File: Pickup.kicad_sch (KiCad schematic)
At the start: 38 parts, among them U401 PCM1808, U402 PCM1808, U403 PCM1808

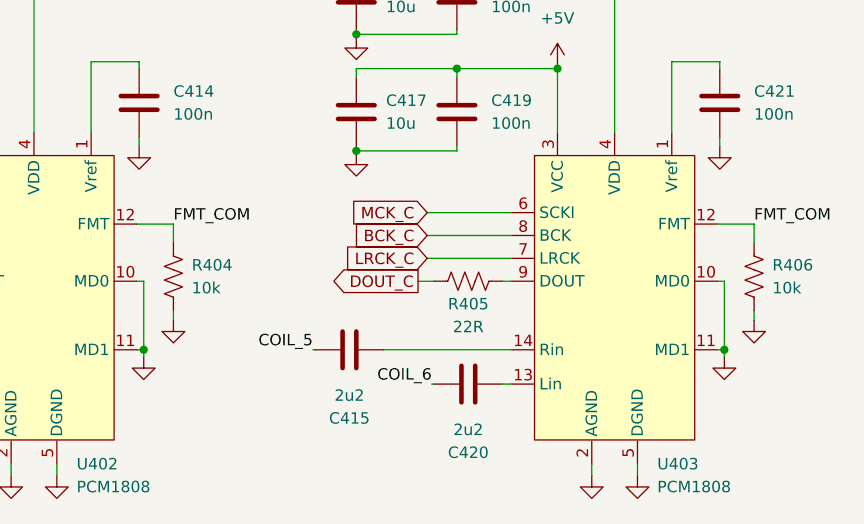
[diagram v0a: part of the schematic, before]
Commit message: installed Semtech LLCC68 RF driver
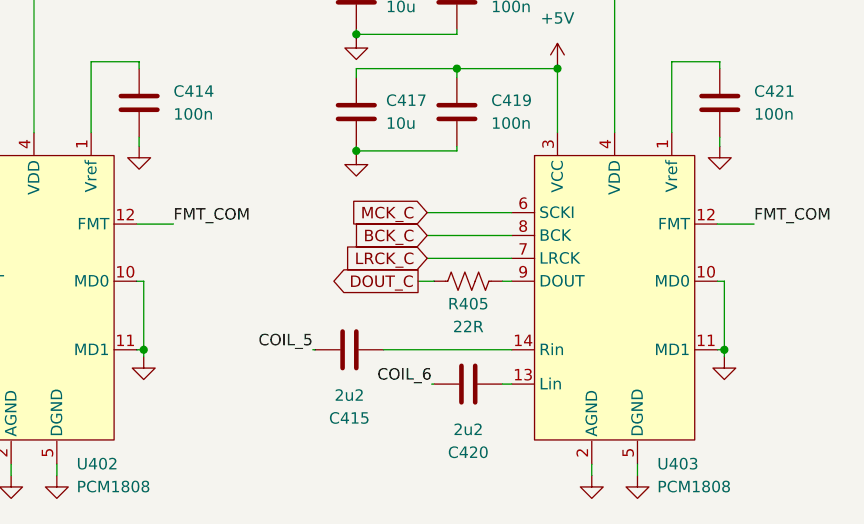
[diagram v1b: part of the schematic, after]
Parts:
- removed R404, R406: 10k, symbol Device:R_US

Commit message: LEDs and footprints
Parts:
- C406, C407, C408, C413, C415, C420: footprint (none) -> Capacitor_SMD:C_0805_2012Metric
- JP401: footprint (none) -> Jumper:SolderJumper-2_P1.3mm_Open_TrianglePad1.0x1.5mm
- L401, L402, L403, L404, L405, L406: footprint (none) -> Inductor_THT:L_Radial_L8.0mm_W8.0mm_P5.00mm_Neosid_SD8
- NT401: footprint (none) -> NetTie:NetTie-2_SMD_Pad0.5mm
- R401, R402, R403, R405: footprint (none) -> Resistor_SMD:R_0805_2012Metric
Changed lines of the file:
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@@
 			)
 		)
-		(property "Footprint" ""
+		(property "Footprint" "Resistor_SMD:R_0805_2012Metric"
 			(at 230.124 93.472 90)
 			(effects
@@
 			)
 		)
-		(property "Footprint" ""
+		(property "Footprint" "Inductor_THT:L_Radial_L8.0mm_W8.0mm_P5.00mm_Neosid_SD8"
 			(at 40.894 85.344 0)
 			(effects
@@
 			)
 		)
-		(property "Footprint" ""
+		(property "Footprint" "Resistor_SMD:R_0805_2012Metric"
 			(at 100.33 94.234 90)
 			(effects
@@
 			)
 		)
-		(property "Footprint" ""
+		(property "Footprint" "Jumper:SolderJumper-2_P1.3mm_Open_TrianglePad1.0x1.5mm"
 			(at 37.084 106.426 0)
 			(effects
@@
 			)
 		)
-		(property "Footprint" ""
+		(property "Footprint" "Resistor_SMD:R_0805_2012Metric"
 			(at 132.842 94.996 90)
 			(effects
@@
 			)
 		)
-		(property "Footprint" ""
+		(property "Footprint" "Resistor_SMD:R_0805_2012Metric"
 			(at 165.608 93.472 90)
 			(effects
@@
 			)
 		)
-		(property "Footprint" ""
+		(property "Footprint" "Inductor_THT:L_Radial_L8.0mm_W8.0mm_P5.00mm_Neosid_SD8"
 			(at 40.386 68.326 0)
 			(effects
@@
 			)
 		)
-		(property "Footprint" ""
+		(property "Footprint" "Inductor_THT:L_Radial_L8.0mm_W8.0mm_P5.00mm_Neosid_SD8"
 			(at 40.386 59.436 0)
 			(effects
@@
 			)
 		)
-		(property "Footprint" ""
+		(property "Footprint" "Capacitor_SMD:C_0805_2012Metric"
 			(at 226.06 104.9528 0)
 			(effects
@@
 			)
 		)
-		(property "Footprint" ""
+		(property "Footprint" "Capacitor_SMD:C_0805_2012Metric"
 			(at 148.336 101.1428 0)
 			(effects
@@
 			)
 		)
-		(property "Footprint" ""
+		(property "Footprint" "Capacitor_SMD:C_0805_2012Metric"
 			(at 212.852 101.1428 0)
 			(effects
@@
 			)
 		)
-		(property "Footprint" ""
+		(property "Footprint" "Capacitor_SMD:C_0805_2012Metric"
 			(at 96.266 105.7148 0)
 			(effects
@@
 			)
 		)
-		(property "Footprint" ""
+		(property "Footprint" "Capacitor_SMD:C_0805_2012Metric"
 			(at 83.058 101.9048 0)
 			(effects
@@
 			)
 		)
-		(property "Footprint" ""
+		(property "Footprint" "Capacitor_SMD:C_0805_2012Metric"
 			(at 161.544 104.9528 0)
 			(effects
@@
 			)
 		)
-		(property "Footprint" ""
+		(property "Footprint" "NetTie:NetTie-2_SMD_Pad0.5mm"
 			(at 41.402 94.488 0)
 			(effects
@@
 			)
 		)
-		(property "Footprint" ""
+		(property "Footprint" "Inductor_THT:L_Radial_L8.0mm_W8.0mm_P5.00mm_Neosid_SD8"
 			(at 40.894 76.962 0)
 			(effects
@@
 			)
 		)
-		(property "Footprint" ""
+		(property "Footprint" "Inductor_THT:L_Radial_L8.0mm_W8.0mm_P5.00mm_Neosid_SD8"
 			(at 40.386 51.054 0)
 			(effects
@@
 			)
 		)
-		(property "Footprint" ""
+		(property "Footprint" "Inductor_THT:L_Radial_L8.0mm_W8.0mm_P5.00mm_Neosid_SD8"
 			(at 39.878 42.418 0)
 			(effects

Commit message: op amp input stage
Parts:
- removed L401, L402, L403, L404, L405, L406: 7000 winds, Inductor_THT:L_Radial_L8.0mm_W8.0mm_P5.00mm_Neosid_SD8, symbol Device:L
- added C422, C423, C424: 100n, Capacitor_SMD:C_0805_2012Metric, symbol Device:C
- added C425, C426, C427, C428, C429, C430, C431, C432, C433, C434, C435, C436: 1u, Capacitor_SMD:C_0805_2012Metric, symbol Device:C
- added J401: Pickup, Connector_JST:JST_PH_B12B-PH-K_1x12_P2.00mm_Vertical, symbol Connector:Conn_01x12_Pin
- added R404, R406: 100k, Resistor_SMD:R_0805_2012Metric, symbol Device:R_US
- added RN401, RN403, RN405: 10k, Resistor_SMD:R_Array_Concave_4x0603, symbol Device:R_Pack04_Split
- added RN402, RN404, RN406: 33k, Resistor_SMD:R_Array_Concave_4x0603, symbol Device:R_Pack04_Split
- added U404, U405: MCP6009, Package_SO:TSSOP-14_4.4x5mm_P0.65mm, symbol Amplifier_Operational:MCP604
- NT401: value COIL_GND -> VGD
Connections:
- net +5V: now also C422.1, C423.1, R404.1, U404.4 (V+), U405.4 (V+)
- net COIL_1: now also RN402.2 (R2.1), U404.1
- net COIL_2: now also RN402.5 (R4.2), U404.7
- net COIL_3: now also RN404.2 (R2.1), U404.8
- net COIL_4: now also RN404.5 (R4.2), U404.14
- net COIL_5: now also RN406.2 (R2.1), U405.1
- net COIL_6: now also RN406.5 (R4.2), U405.7
- net GND: now also C422.2, C423.2, C424.2, R406.2, U404.11 (V-), U405.11 (V-); no longer NT401.2
- net COIL_COM renamed VGND
- net VGND: now also RN402.1 (R1.1), RN402.6 (R3.2), RN404.1 (R1.1), RN404.6 (R3.2), RN406.1 (R1.1), RN406.6 (R3.2), U405.8, U405.9 (-)
- new net: C424.1, R404.2, R406.1, U405.10 (+), U405.12 (+)
- new net: RN401.1 (R1.1), RN402.7 (R2.2), U404.2 (-)
- new net: C431.2, RN403.6 (R3.2)
- new net: RN401.4 (R4.1), RN402.3 (R3.1), U404.5 (+)
- new net: RN401.3 (R3.1), RN402.4 (R4.1), U404.6 (-)
- new net: RN403.2 (R2.1), RN404.8 (R1.2), U404.10 (+)
- new net: C433.2, RN403.7 (R2.2)
- new net: C427.2, RN401.6 (R3.2)
- new net: C428.2, RN401.5 (R4.2)
- new net: RN405.1 (R1.1), RN406.7 (R2.2), U405.2 (-)
- new net: NT401.2, U405.13 (-), U405.14
- new net: C426.2, RN401.7 (R2.2)
- new net: RN401.2 (R2.1), RN402.8 (R1.2), U404.3 (+)
- new net: C429.2, RN405.6 (R3.2)
- new net: RN405.3 (R3.1), RN406.4 (R4.1), U405.6 (-)
- new net: C435.2, RN405.7 (R2.2)
- new net: RN403.3 (R3.1), RN404.4 (R4.1), U404.13 (-)
- new net: RN403.4 (R4.1), RN404.3 (R3.1), U404.12 (+)
- new net: C434.2, RN403.5 (R4.2)
- new net: RN405.2 (R2.1), RN406.8 (R1.2), U405.3 (+)
- new net: C432.2, RN403.8 (R1.2)
- new net: RN403.1 (R1.1), RN404.7 (R2.2), U404.9 (-)
- new net: RN405.4 (R4.1), RN406.3 (R3.1), U405.5 (+)
- new net: C436.2, RN405.5 (R4.2)
- new net: C425.2, RN401.8 (R1.2)
- new net: C430.2, RN405.8 (R1.2)
- new net COIL1+: C425.1, J401.1 (Pin_1)
- new net COIL1-: C426.1, J401.2 (Pin_2)
- new net COIL2+: C427.1, J401.3 (Pin_3)
- new net COIL2-: C428.1, J401.4 (Pin_4)
- new net COIL3+: C432.1, J401.5 (Pin_5)
- new net COIL3-: C433.1, J401.6 (Pin_6)
- new net COIL4+: C431.1, J401.7 (Pin_7)
- new net COIL4-: C434.1, J401.8 (Pin_8)
- new net COIL5+: C430.1, J401.9 (Pin_9)
- new net COIL5-: C435.1, J401.10 (Pin_10)
- new net COIL6+: C429.1, J401.11 (Pin_11)
- new net COIL6-: C436.1, J401.12 (Pin_12)
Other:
- note added: "Audio ADCs (3x PCM1808)"
- note added: "Coil Preamp"
- note added: "These are just soldered to either end of each coil"
- moved on the sheet: C401, C402, C403, C404, C405, C406, C407, C408, C409, C410, C411, C412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

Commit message: resistor array routing fix
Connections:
- net COIL_1: now also RN402.6 (R3.2), U404.7; no longer RN402.2 (R2.1), U404.1
- net COIL_2: now also RN402.8 (R1.2), U404.1; no longer RN402.5 (R4.2), U404.7
- net COIL_3: now also RN404.6 (R3.2), U404.14; no longer RN404.2 (R2.1), U404.8
- net COIL_4: now also RN404.8 (R1.2), U404.8; no longer RN404.5 (R4.2), U404.14
- net COIL_5: now also RN406.6 (R3.2), U405.7; no longer RN406.2 (R2.1), U405.1
- net COIL_6: now also RN406.8 (R1.2), U405.1; no longer RN406.5 (R4.2), U405.7
- net VGND: now also RN402.5 (R4.2), RN402.7 (R2.2), RN404.5 (R4.2), RN404.7 (R2.2), RN406.5 (R4.2), RN406.7 (R2.2); no longer RN402.1 (R1.1), RN402.6 (R3.2), RN404.1 (R1.1), RN404.6 (R3.2), RN406.1 (R1.1), RN406.6 (R3.2)
- net at C431.2: now also RN403.2 (R2.1); no longer RN403.6 (R3.2)
- net at RN403.7 (R2.2): now also RN404.2 (R2.1), U404.10 (+); no longer C433.2
- net at RN401.6 (R3.2): now also RN402.3 (R3.1), U404.6 (-); no longer C427.2
- net at RN401.5 (R4.2): now also RN402.4 (R4.1), U404.5 (+); no longer C428.2
- net at RN401.7 (R2.2): now also RN402.2 (R2.1), U404.3 (+); no longer C426.2
- net at C429.2: now also RN405.2 (R2.1); no longer RN405.6 (R3.2)
- net at RN405.7 (R2.2): now also RN406.2 (R2.1), U405.3 (+); no longer C435.2
- net at RN403.5 (R4.2): now also RN404.4 (R4.1), U404.12 (+); no longer C434.2
- net at RN403.8 (R1.2): now also RN404.1 (R1.1), U404.9 (-); no longer C432.2
- net at RN405.5 (R4.2): now also RN406.4 (R4.1), U405.5 (+); no longer C436.2
- net at C425.2: now also RN401.4 (R4.1); no longer RN401.8 (R1.2)
- net at C430.2: now also RN405.4 (R4.1); no longer RN405.8 (R1.2)
- new net: C426.2, RN401.3 (R3.1)
- new net: C428.2, RN401.1 (R1.1)
- new net: C427.2, RN401.2 (R2.1)
- new net: C433.2, RN403.3 (R3.1)
- new net: C435.2, RN405.3 (R3.1)
- new net: RN405.6 (R3.2), RN406.3 (R3.1), U405.6 (-)
- new net: C432.2, RN403.4 (R4.1)
- new net: RN403.6 (R3.2), RN404.3 (R3.1), U404.13 (-)
- new net: RN401.8 (R1.2), RN402.1 (R1.1), U404.2 (-)
- new net: C434.2, RN403.1 (R1.1)
- new net: RN405.8 (R1.2), RN406.1 (R1.1), U405.2 (-)
- new net: C436.2, RN405.1 (R1.1)
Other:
- moved on the sheet: C425, C426, C427, C428, C429, C430, C431, C432, C433, C434, C435, C436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
